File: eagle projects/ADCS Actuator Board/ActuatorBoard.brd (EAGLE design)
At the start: 91 x 91 mm, 259 parts, among them J4 OSTVN08A150, J5 OSTVN08A150, J6 OSTVN08A150, U10 TVS991, U11 BD6210F-E2, U12 ADS7841E_2K5, U13 ADS7841E_2K5, U15 TLV9051IDCKR, U16 BD6210F-E2, U17 DRV10970_MOTOR_DRIVERDRV10970, U18 DRV10970_MOTOR_DRIVERDRV10970, U19 TLV9051IDCKR, U20 DRV10970_MOTOR_DRIVERDRV10970, U21 TLV9051IDCKR, U22 BD6210F-E2, U23 TLV9051IDCKR, U24 TLV9051IDCKR, U25 ADS7841E_2K5, U26 TLV9051IDCKR, U27 ADS7841E_2K5, U28 TLV9051IDCKR, U29 TLV9051IDCKR, U30 TLV9051IDCKR, U31 TLV9051IDCKR, U32 TLV9051IDCKR, U4 ADS7841E_2K5, U6 TLV9051IDCKR, U7 TVS991, U8 TVS991, U9 ADS7841E_2K5

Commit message: moved a bunch of digital shit around (work in progress). going to sleep now
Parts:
- removed TP1, TP13, TP17, TP9: TESTPOINT, my_library:TP_P76H50
- added J7: (no value), my_library:2POL254
- moved D13 21.9 mm to (23.2, 2.86), turned to 90 degrees
- moved D15 21.8 mm to (12.4, 2.86), turned to 90 degrees
- moved D14 20.7 mm to (17.8, 2.86), turned to 90 degrees
- moved R69 18.4 mm to (13.3, 5.71), turned to 180 degrees
- moved R4 18.0 mm to (18.4, 36.8)
- moved R6 17.3 mm to (22.9, 52.1), turned to 180 degrees
- moved R63 16.9 mm to (22.2, 5.71), turned to 180 degrees
- moved R68 16.8 mm to (13.3, 6.99), turned to 0 degrees
- moved R66 16.5 mm to (17.8, 5.71), turned to 180 degrees
- moved TP10 16.3 mm to (14.0, 28.9)
- moved C113 15.3 mm to (13.3, 8.26), turned to 0 degrees
- moved R62 15.2 mm to (22.2, 6.99), turned to 0 degrees
- moved TP3 15.2 mm to (7.62, 51.1), turned to 90 degrees
- moved R65 14.7 mm to (17.8, 6.99), turned to 0 degrees
- moved C81 14.7 mm to (22.9, 50.8), turned to 180 degrees
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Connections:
- removed net N$37: TP1.1, U4.3
- removed net N$48: TP9.1, U13.3
- removed net N$59: TP13.1, U25.3
- removed net N$67: TP17.1, U27.3
- net X+_0_DEGREES: now also U25.3; no longer U25.2
- net X-_0_DEGREES: now also U13.3; no longer U13.2
- net Y+_0_DEGREES: now also U27.3; no longer U27.2
- net Y-_0_DEGREES: now also U4.3; no longer U4.2
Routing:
- net N$24: track 22.8 -> 1.95 mm
- net !CS!_SUN_Y-: track 48.2 -> 64.3 mm, vias 2 -> 1
- net N$37: track 16.1 -> 0.00 mm
- net +3V3: track 227.1 -> 243.0 mm
- net GND: track 216.0 -> 230.7 mm
- net N$22: track 17.5 -> 3.34 mm
- net N$48: track 12.2 -> 0.00 mm
- net N$67: track 12.0 -> 0.00 mm
- net N$59: track 9.78 -> 0.00 mm
- net Y+_0_DEGREES: track 17.2 -> 8.73 mm
- net N$25: track 15.8 -> 7.45 mm
- net N$4: track 14.5 -> 6.35 mm
- net N$33: track 14.2 -> 7.24 mm
- net Y-_240_DEGREES: track 24.3 -> 17.7 mm
- net UCB0_SPI_MISO: track 103.5 -> 109.7 mm
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
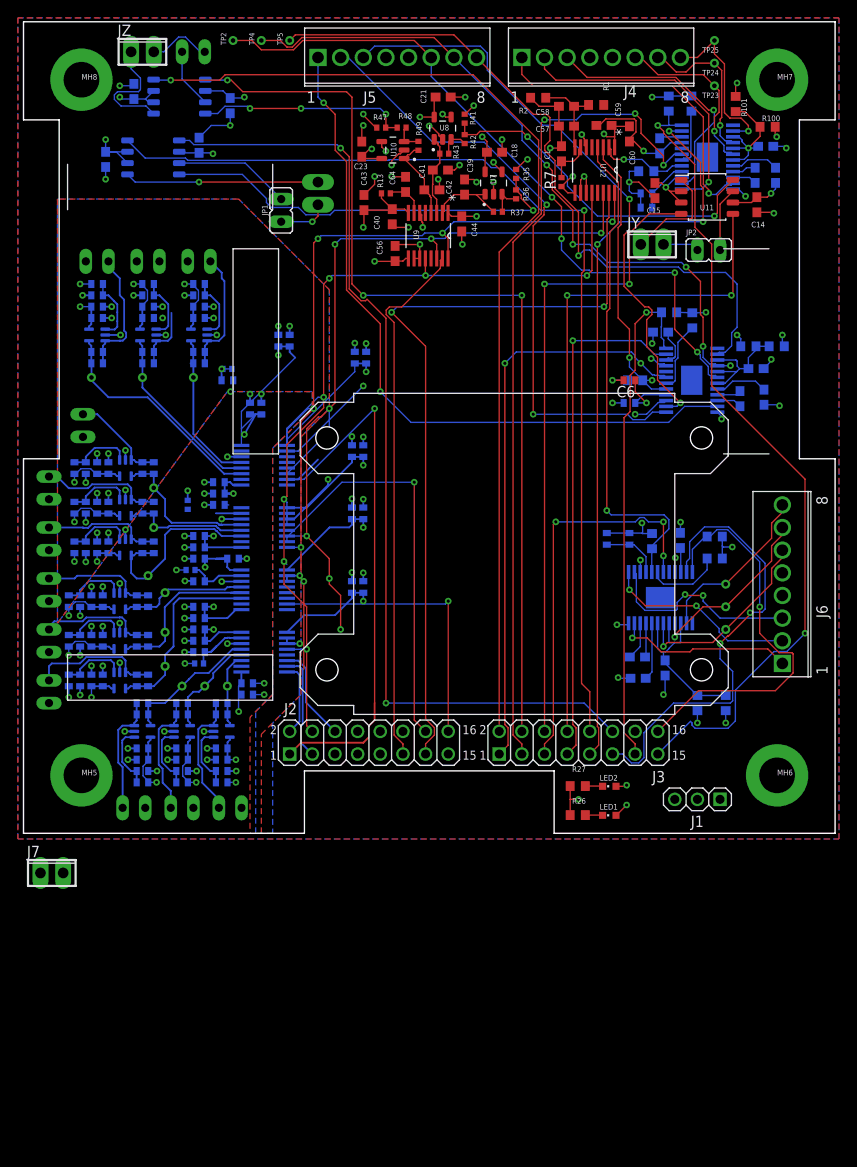
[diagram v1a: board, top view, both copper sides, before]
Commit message: finished rearranging analog side for minimal a/d ground bridge spacing
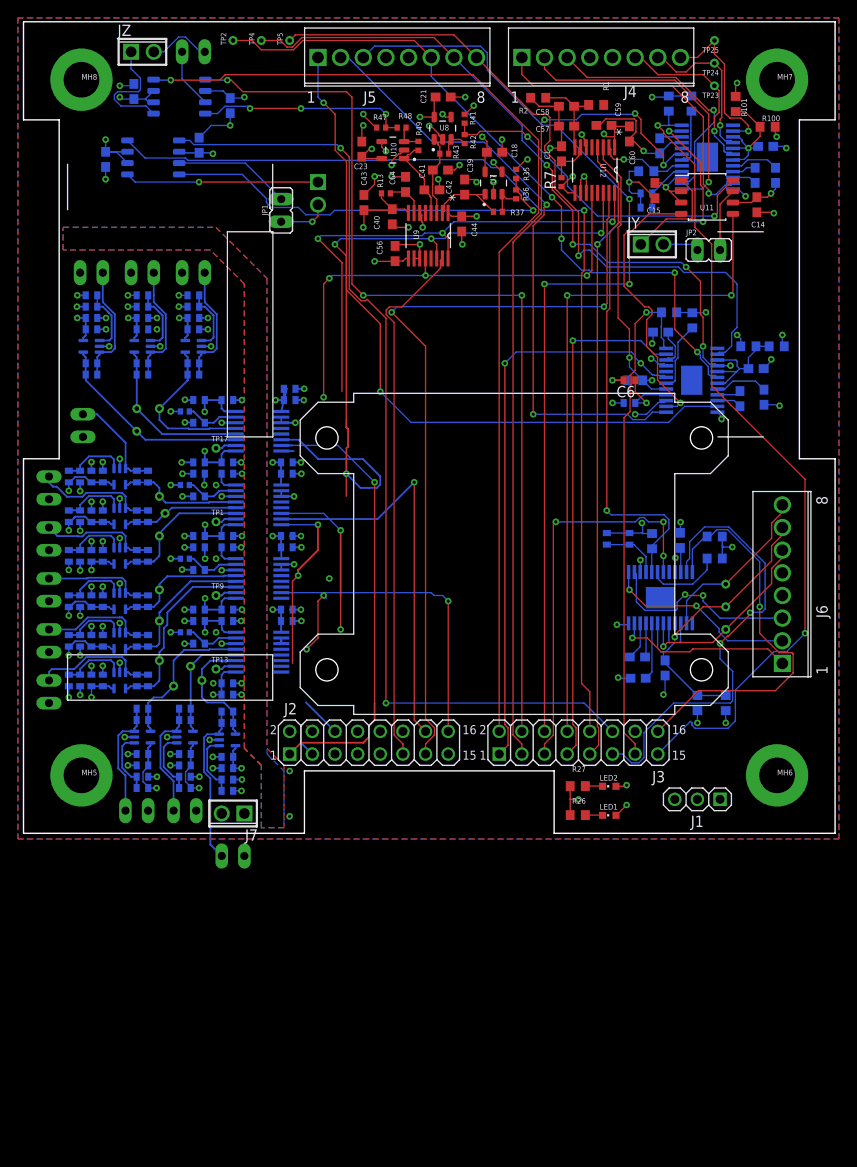
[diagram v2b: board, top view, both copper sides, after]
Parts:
- added TP1, TP13, TP17, TP9: TESTPOINT, my_library:TP_P76H50
- moved J7 21.4 mm to (23.5, 2.22), turned to 180 degrees
- moved C28 11.1 mm to (19.7, 48.6), turned to 0 degrees
- moved C80 9.81 mm to (29.8, 48.6), turned to 180 degrees
- moved C65 9.66 mm to (22.9, 48.6), turned to 180 degrees
- moved C66 9.23 mm to (19.7, 41.6), turned to 0 degrees
- moved C77 8.94 mm to (29.5, 33.3), turned to 180 degrees
- moved C94 8.94 mm to (29.5, 25.1), turned to 180 degrees
- moved C50 8.67 mm to (29.5, 41.6), turned to 180 degrees
- moved C93 8.24 mm to (29.5, 23.8), turned to 180 degrees
- moved C76 8.24 mm to (29.5, 32.1), turned to 180 degrees
- moved C79 8.09 mm to (29.8, 49.8), turned to 180 degrees
- moved TP3 7.89 mm to (12.7, 45.1)
- moved C49 7.73 mm to (29.5, 40.3), turned to 180 degrees
- moved R6 6.74 mm to (18.1, 47.3), turned to 0 degrees
- moved C78 6.55 mm to (22.9, 41.6), turned to 180 degrees
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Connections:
- new net N$1: TP1.1, U13.2
- new net N$2: TP9.1, U25.2
- new net N$3: TP13.1, U27.2
- new net N$9: TP17.1, U4.2
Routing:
- net +3V3: track 243.0 -> 183.6 mm, vias 44 -> 46
- net UCB0_SPI_MISO: track 109.7 -> 62.5 mm, vias 7 -> 6
- net UCB0_SPI_CLK: track 110.2 -> 81.4 mm, vias 6 -> 5
- net GND: track 230.7 -> 214.0 mm, vias 131 -> 136
- net !CS!_SUN_Y-: track 64.3 -> 51.9 mm
- net !CS!_SUN_Y+: track 12.0 -> 3.97 mm
- net N$33: track 7.24 -> 13.6 mm
- net Y+_0_DEGREES: track 8.73 -> 14.2 mm
- net X-_0_DEGREES: track 21.4 -> 16.6 mm
- net N$60: track 14.3 -> 18.6 mm
- net N$24: track 1.95 -> 6.13 mm
- net X-_240_DEGREES: track 17.4 -> 14.6 mm
- net N$22: track 3.34 -> 5.99 mm
- net Y-_0_DEGREES: track 25.4 -> 22.9 mm
- net N$9: track 0.00 -> 2.34 mm
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
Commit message: fixed silkscreen fiasco
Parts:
- removed D1, D10, D11, D12, D13, D14, D15, D3, D5, D7, D8, D9: SFH2430, my_library:JP1Y_LED_SCREEN
- added J10, J11, J12, J13, J14, J15, J16, J17, J18, J8, J9: (no value), my_library:2POL254
- moved J7 61.5 mm to (13.3, 62.9), flipped to the bottom, turned to 0 degrees
- moved MX 2.31 mm to (25.1, 43.8)
- moved C79 1.31 mm to (29.5, 48.6)
- moved C80 1.31 mm to (29.5, 49.8)
- moved JP1 0.64 mm to (29.5, 69.8)
- flipped JX to the top, turned to 90 degrees
- turned JY to 180 degrees
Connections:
- removed net N$33: C100.1, D3.1, R31.1, U23.3
- removed net N$60: C98.1, D13.1, R64.1, U30.3
- new net N$23: C100.1, J7.2, R31.1, U23.3
- new net N$37: C98.1, J12.2, R64.1, U30.3
- net GND: now also J10.1, J11.1, J12.1, J13.1, J14.1, J15.1, J16.1, J17.1, J18.1, J7.1, J8.1, J9.1; no longer D1.2, D10.2, D11.2, D12.2, D13.2, D14.2, D15.2, D3.2, D5.2, D7.2, D8.2, D9.2
- net N$29: now also J8.2; no longer D1.1
- net N$35: now also J9.2; no longer D5.1
- net N$38: now also J15.2; no longer D7.1
- net N$44: now also J14.2; no longer D8.1
- net N$46: now also J13.2; no longer D9.1
- net N$49: now also J18.2; no longer D10.1
- net N$55: now also J17.2; no longer D11.1
- net N$57: now also J16.2; no longer D12.1
- net N$63: now also J11.2; no longer D14.1
- net N$65: now also J10.2; no longer D15.1
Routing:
- net N$60: track 18.6 -> 0.00 mm
- net N$37: track 0.00 -> 15.8 mm
- net N$23: track 0.00 -> 14.9 mm
- net N$33: track 13.6 -> 0.00 mm
- net OUT2_Y: track 4.07 -> 6.61 mm, vias 0 -> 1
- net +3V3: track 183.6 -> 186.1 mm
- net N$55: track 13.3 -> 15.6 mm
- net N$46: track 11.6 -> 9.33 mm
- net OUT2_X: track 5.66 -> 7.57 mm, vias 1 -> 2
- net N$63: track 13.7 -> 15.3 mm
- net N$49: track 15.0 -> 16.5 mm
- net N$29: track 13.8 -> 15.3 mm
- net N$57: track 12.7 -> 14.1 mm
- net N$35: track 13.6 -> 14.9 mm
- net OUT1_Y: track 11.8 -> 10.6 mm, vias 0 -> 1
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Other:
- board text added: "C72"
- board text added: "U15"
- board text added: "U19"
- board text added: "U21"
- board text added: "U23"
- board text added: "U24"
- board text added: "U26"
- board text added: "U28"
- board text added: "U29"
- board text added: "U30"
- board text added: "U31"
- board text added: "U32"
- board text added: "U6"

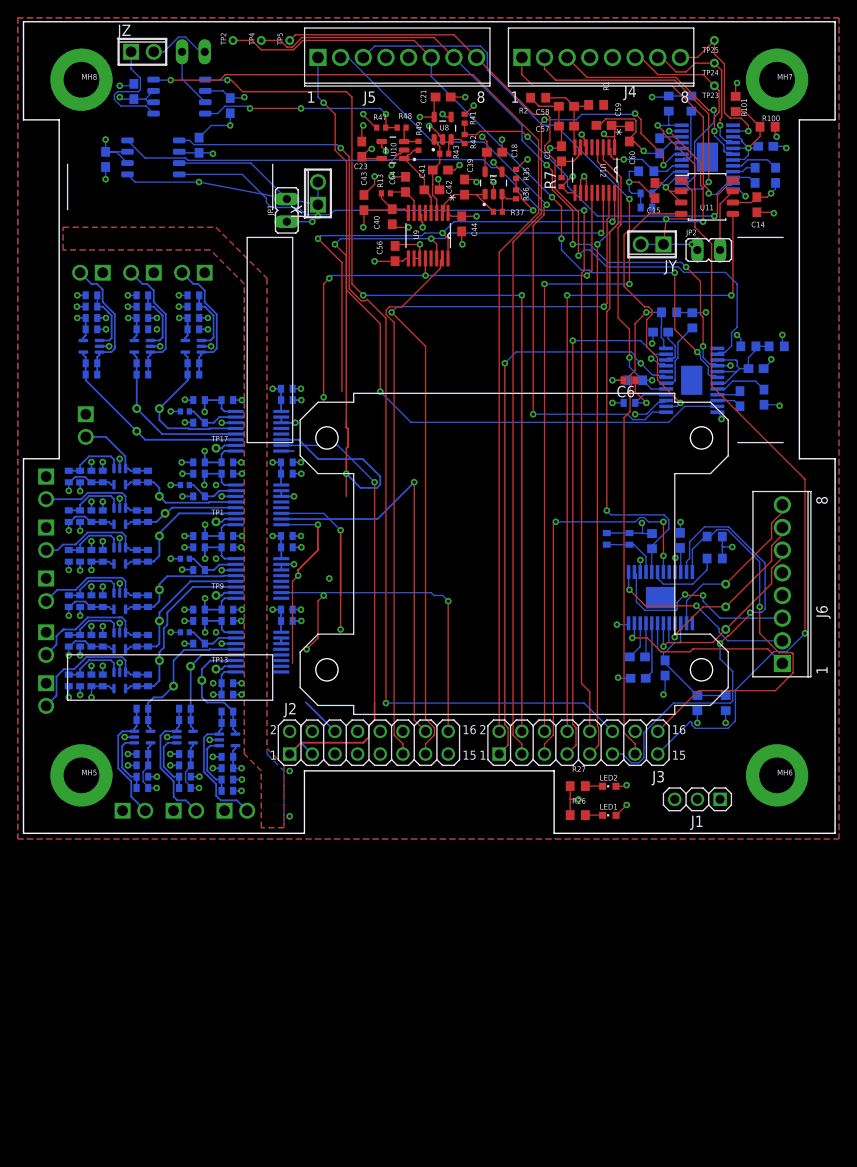
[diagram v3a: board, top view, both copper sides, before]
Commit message: Rerouted traces no drc errors except keepout around 1 TP
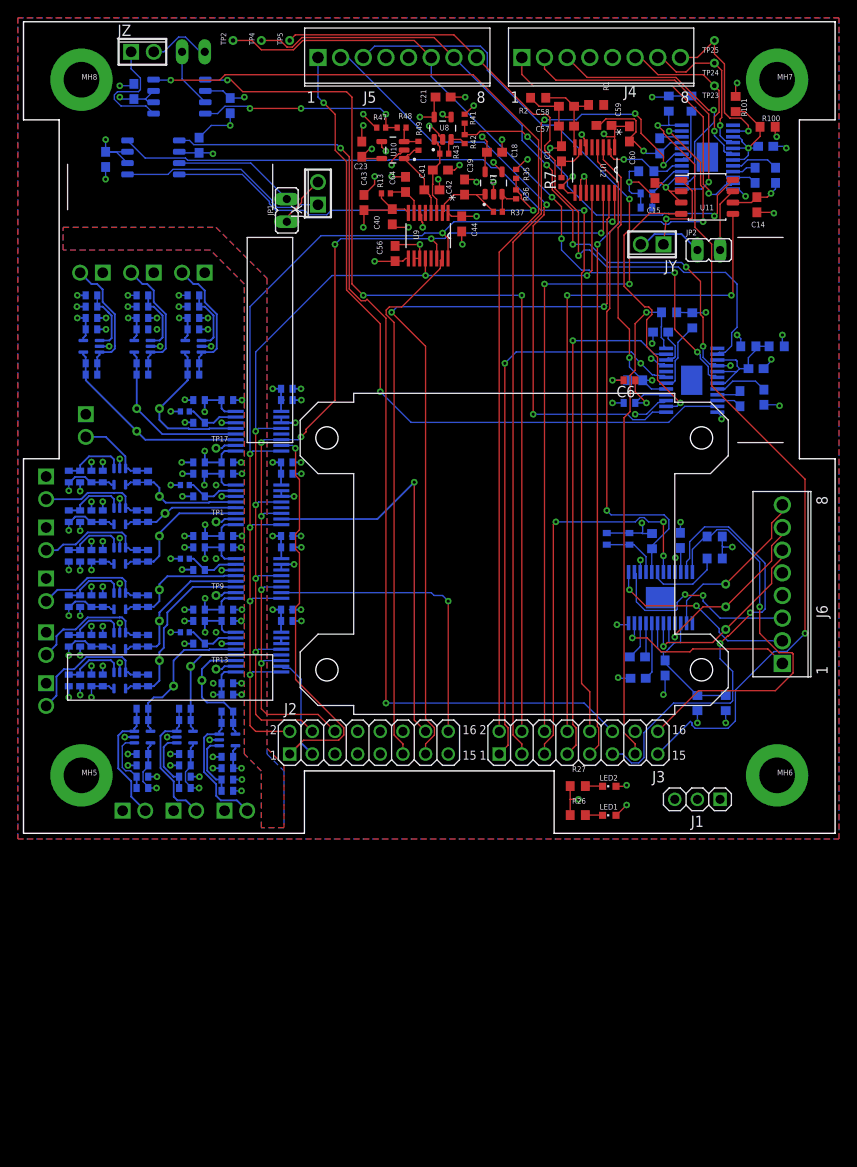
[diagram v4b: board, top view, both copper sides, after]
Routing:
- net UCB0_SPI_MISO: track 62.5 -> 111.9 mm
- net UCB0_SPI_CLK: track 81.4 -> 117.3 mm, vias 5 -> 6
- net !CS!_SUN_Y-: track 51.9 -> 43.8 mm
- net !CS!_SUN_Y+: track 3.97 -> 11.7 mm
- net UCB0_SPI_MOSI: track 108.2 -> 111.6 mm, vias 7 -> 8
- net OUT1_X: track 22.0 -> 23.6 mm, vias 1 -> 0
- net OUT2_X: track 7.57 -> 5.89 mm, vias 2 -> 0
- net Y-_120_DEGREES: track 20.3 -> 18.7 mm
- net OUT2_Y: track 6.61 -> 7.57 mm, vias 1 -> 0
- net X-_240_DEGREES: track 14.6 -> 14.0 mm
- net GND: vias 136 -> 134

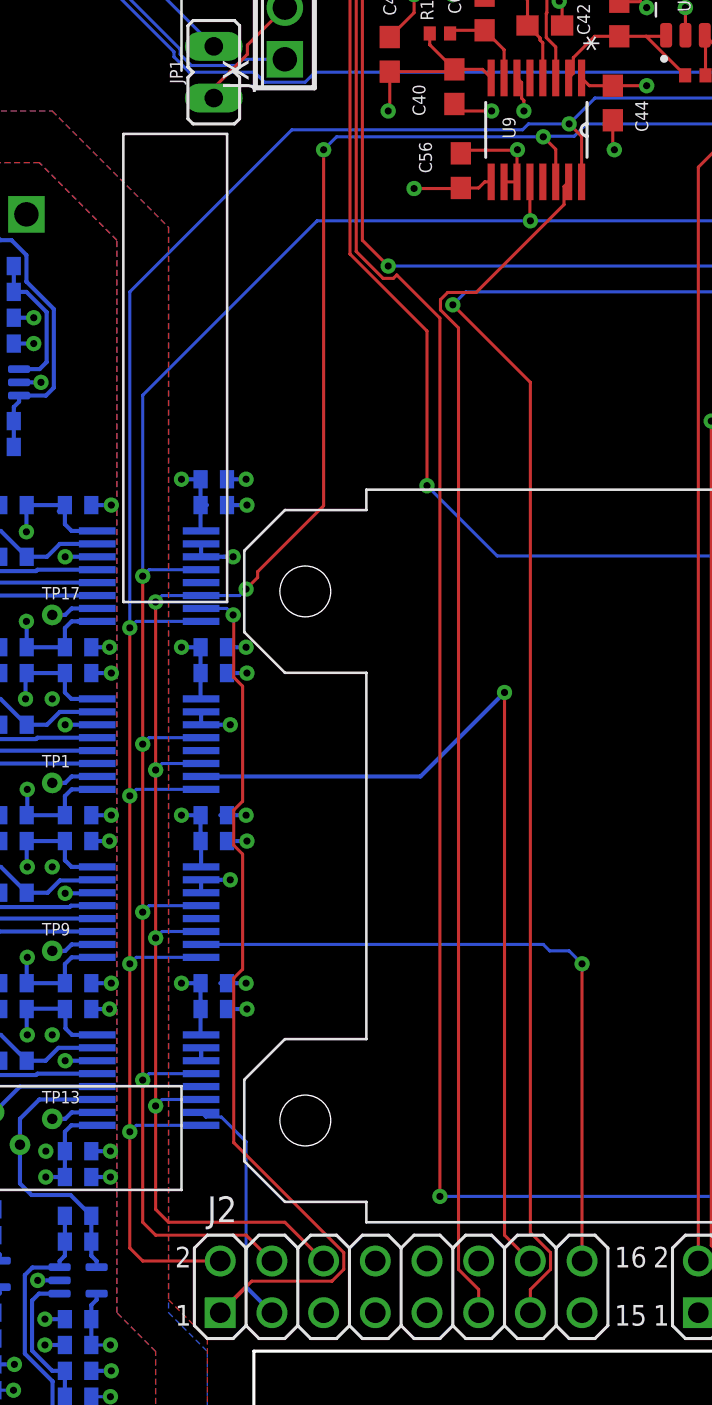
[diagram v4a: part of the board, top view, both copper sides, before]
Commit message: moved clk traces to be over ground plane
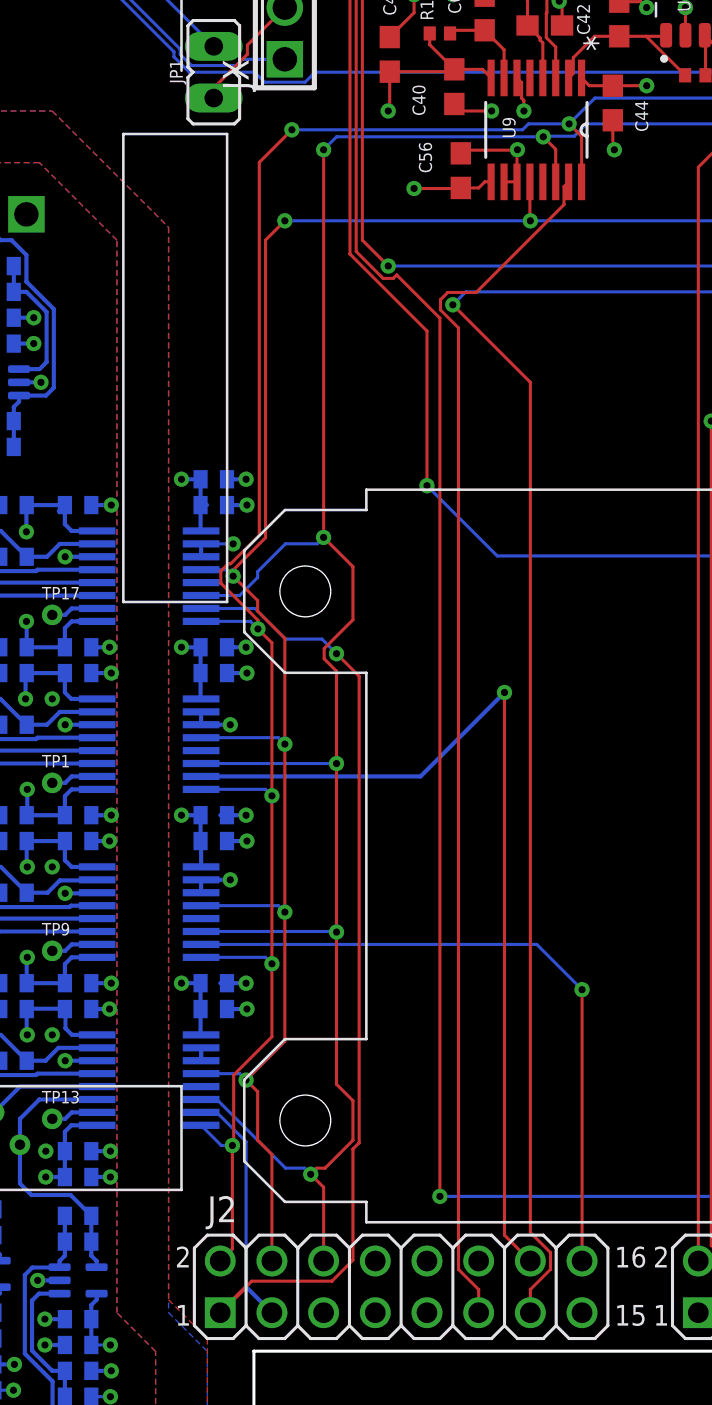
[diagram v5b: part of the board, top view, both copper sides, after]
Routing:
- net UCB0_SPI_MOSI: track 111.6 -> 122.8 mm, vias 8 -> 7
- net UCB0_SPI_CLK: track 117.3 -> 111.1 mm, vias 6 -> 7
- net UCB0_SPI_MISO: track 111.9 -> 108.7 mm, vias 6 -> 7
- net !CS!_SUN_Y-: track 43.8 -> 45.6 mm
- net !CS!_SUN_X+: track 33.7 -> 33.0 mm
